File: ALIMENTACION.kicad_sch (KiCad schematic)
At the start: 12 parts, among them J5 5V_IN, U9 AP63203WU

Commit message: routing
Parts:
- added J20: 3V_IN, Connector_PinHeader_2.54mm:PinHeader_1x02_P2.54mm_Vertical, symbol Connector_Generic:Conn_01x02
- added R37, R38: 0, Resistor_SMD:R_0805_2012Metric, symbol Device:R
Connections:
- net +3.3V: now also R37.2, R38.2; no longer C30.1, C31.1, L2.2, U9.1 (FB)
- net GND: now also J20.2 (Pin_2)
- new net 3.3V_EXT: J20.1 (Pin_1), R37.1
- new net BUCK_3.3V: C30.1, C31.1, L2.2, R38.1, U9.1 (FB)
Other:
- moved on the sheet: C22

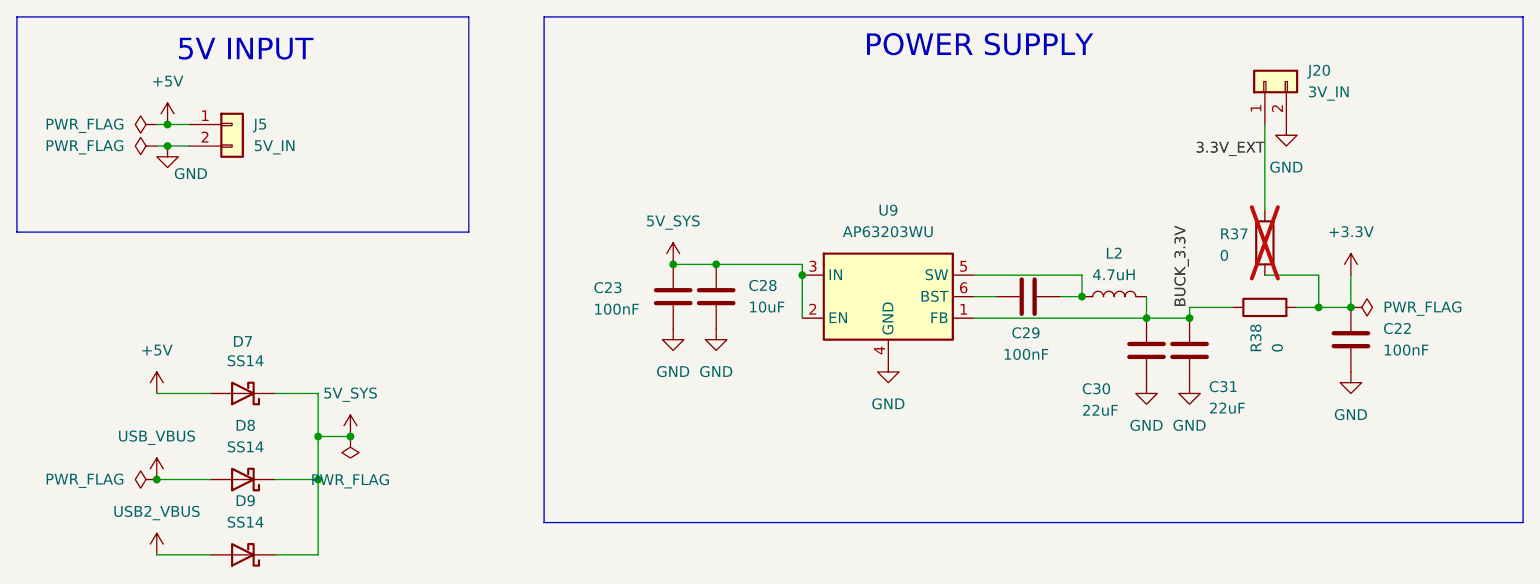
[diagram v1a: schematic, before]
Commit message: buck remplazado por regulador lineal
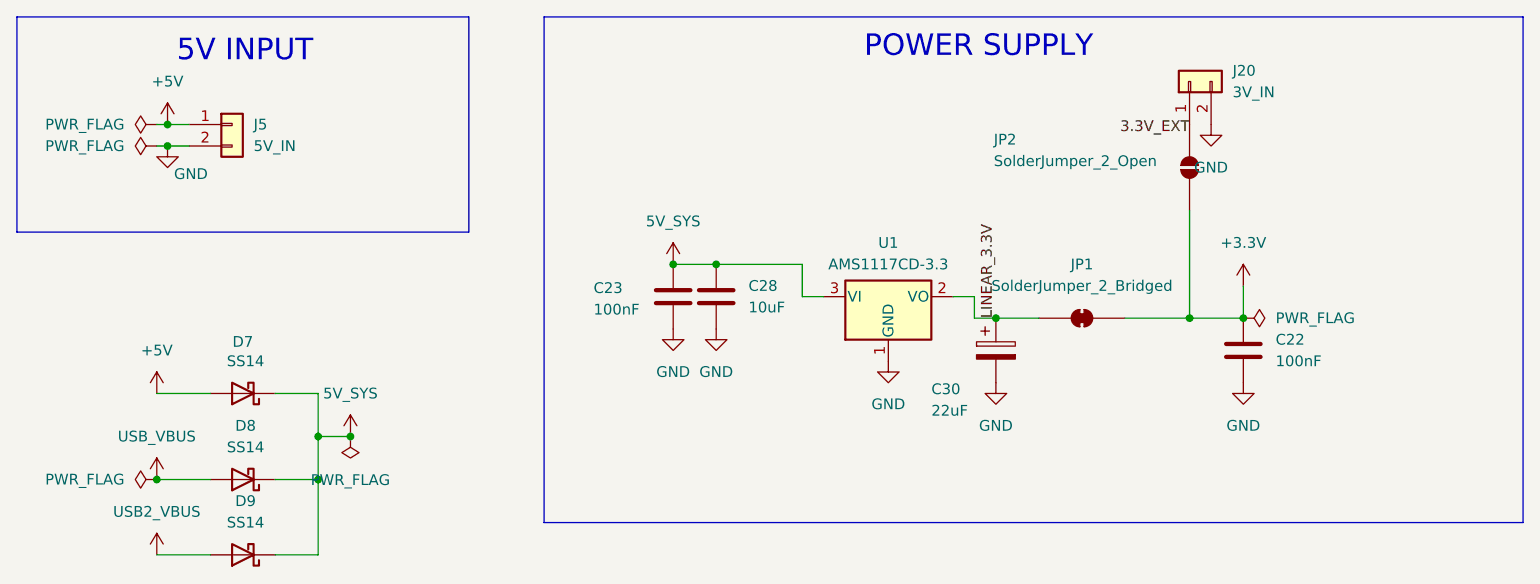
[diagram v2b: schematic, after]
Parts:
- removed C29: 100nF, Capacitor_SMD:C_0603_1608Metric, symbol Device:C
- removed C31: 22uF, Capacitor_SMD:C_0805_2012Metric, symbol Device:C
- removed L2: 4.7uH, Inductor_SMD:L_Changjiang_FXL0530, symbol Device:L
- removed R37, R38: 0, Resistor_SMD:R_0805_2012Metric, symbol Device:R
- removed U9: AP63203WU, Package_TO_SOT_SMD:TSOT-23-6, symbol Regulator_Switching:AP63203WU
- added JP1: SolderJumper_2_Bridged, Jumper:SolderJumper-2_P1.3mm_Bridged_RoundedPad1.0x1.5mm, symbol Jumper:SolderJumper_2_Bridged
- added JP2: SolderJumper_2_Open, Jumper:SolderJumper-2_P1.3mm_Open_RoundedPad1.0x1.5mm, symbol Jumper:SolderJumper_2_Open
- added U1: AMS1117CD-3.3, Package_TO_SOT_SMD:TO-252-3_TabPin2, symbol Regulator_Linear:AMS1117CD-3.3
- C30: footprint Capacitor_SMD:C_0805_2012Metric -> Capacitor_Tantalum_SMD:CP_EIA-3528-21_Kemet-B; symbol Device:C -> Device:C_Polarized; LCSC PN C45783 -> C117030; MPN CL21A226MAQNNNE -> T491B226K010AT; Manufacturer Samsung Electro-Mechanics -> KEMET; Manufacturer Part CL21A226MAQNNNE -> T491B226K010AT
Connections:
- net +3.3V: now also JP1.2 (B), JP2.2 (B)
- net 3.3V_EXT: no longer J20.1 (Pin_1)
- net 5V_SYS: now also U1.3 (VI)
- net GND: now also U1.1 (GND)
- net BUCK_3.3V renamed LINEAR_3.3V
- net LINEAR_3.3V: now also JP1.1 (A), U1.2 (VO)
- new net: J20.1 (Pin_1), JP2.1 (A)
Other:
- moved on the sheet: C22, J20

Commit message: removed usb_uart0
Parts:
- removed D8: SS14, Diode_SMD:D_SMA, symbol Diode:SS14

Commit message: fixes
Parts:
- JP1: now left out of the parts list
- U1: LCSC PN (none) -> C841796; MPN (none) -> AMS1117CD-3.3; Manufacturer (none) -> Advanced Monolithic Systems
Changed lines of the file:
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@@
 		(body_style 1)
 		(exclude_from_sim no)
-		(in_bom yes)
+		(in_bom no)
 		(on_board yes)
 		(in_pos_files yes)
@@
 			(hide yes)
 			(show_name no)
+			(do_not_autoplace no)
+			(effects
+				(font
+					(size 1.27 1.27)
+				)
+			)
+		)
+		(property "MPN" "AMS1117CD-3.3"
+			(at 0 0 0)
+			(hide yes)
+			(show_name no)
+			(do_not_autoplace no)
+			(effects
+				(font
+					(size 1.27 1.27)
+				)
+			)
+		)
+		(property "Manufacturer" "Advanced Monolithic Systems"
+			(at 0 0 0)
+			(hide yes)
+			(show_name no)
+			(do_not_autoplace no)
+			(effects
+				(font
+					(size 1.27 1.27)
+				)
+			)
+		)
+		(property "LCSC PN" "C841796"
+			(at 0 0 0)
+			(hide yes)
+			(show_name no)

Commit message: fixes
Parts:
- J20, J5: now left out of the parts list
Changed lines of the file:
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@@
 		(body_style 1)
 		(exclude_from_sim no)
-		(in_bom yes)
-		(on_board yes)
-		(in_pos_files yes)
+		(in_bom no)
+		(on_board yes)
+		(in_pos_files no)
 		(dnp no)
 		(fields_autoplaced yes)
@@
 		(body_style 1)
 		(exclude_from_sim no)
-		(in_bom yes)
-		(on_board yes)
-		(in_pos_files yes)
+		(in_bom no)
+		(on_board yes)
+		(in_pos_files no)
 		(dnp no)
 		(fields_autoplaced yes)

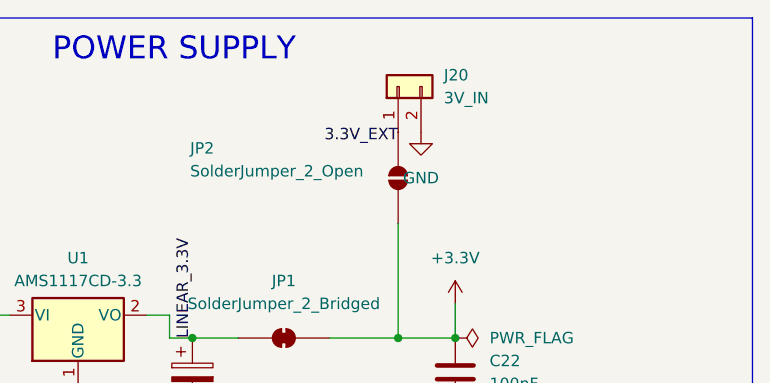
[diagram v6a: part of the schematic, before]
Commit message: Libera paquete JLCPCB SALUS v3
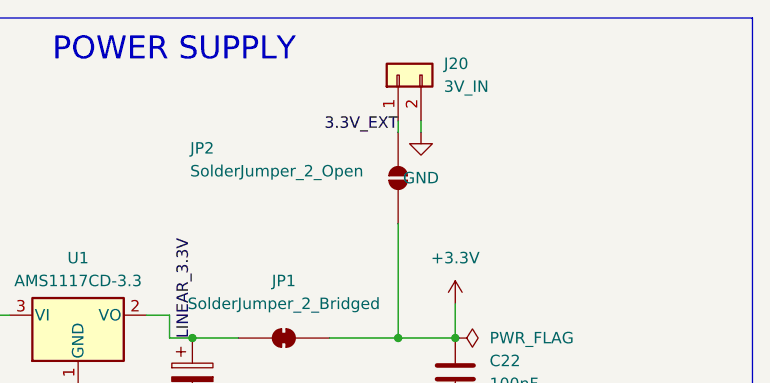
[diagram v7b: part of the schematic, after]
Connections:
- net 3.3V_EXT: now also J20.1 (Pin_1), JP2.1 (A)
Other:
- moved on the sheet: J20
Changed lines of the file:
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@@
+	(wire
+		(pts
+			(xy 167.64 59.69) (xy 167.64 60.96)
+		)
+		(stroke
+			(width 0)
+			(type default)
+		)
+	)
 	(wire
 		(pts
@@
 	(wire
 		(pts
+			(xy 165.1 59.69) (xy 165.1 60.96)
+		)
+		(stroke
+			(width 0)
+			(type default)
+		)
+	)
+	(wire
+		(pts
 			(xy 43.18 63.5) (xy 44.45 63.5)
 		)
@@
 	)
 	(label "3.3V_EXT"
-		(at 165.1 62.23 180)
+		(at 165.1 60.96 180)
 		(effects
 			(font
@@
 	(symbol
 		(lib_id "Connector_Generic:Conn_01x02")
-		(at 165.1 55.88 90)
+		(at 165.1 54.61 90)
 		(unit 1)
 		(body_style 1)
@@
 		(fields_autoplaced yes)
 		(property "Reference" "J20"
-			(at 170.18 54.6099 90)
+			(at 170.18 53.3399 90)
 			(show_name no)
 			(do_not_autoplace no)
@@
 		)
 		(property "Value" "3V_IN"
-			(at 170.18 57.1499 90)
+			(at 170.18 55.8799 90)
 			(show_name no)
 			(do_not_autoplace no)
@@
 		)
 		(property "Footprint" "Connector_PinHeader_2.54mm:PinHeader_1x02_P2.54mm_Vertical"
-			(at 165.1 55.88 0)
+			(at 165.1 54.61 0)
 			(hide yes)
 			(show_name no)
@@
 		)
 		(property "Datasheet" ""
-			(at 165.1 55.88 0)
+			(at 165.1 54.61 0)
 			(hide yes)
 			(show_name no)
@@
 		)
 		(property "Description" "Generic connector, single row, 01x02, script generated (kicad-library-utils/schlib/autogen/connector/)"
-			(at 165.1 55.88 0)
-			(hide yes)
-			(show_name no)
+			(at 165.1 54.61 0)
+			(hide yes)
+			(show_name no)

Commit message: Consolida pasivos Basic y valida filtro de acelerador
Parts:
- C22, C23: LCSC PN C1590 -> C14663; MPN CL10B104KA8NNNC -> CC0603KRX7R9BB104; Manufacturer Samsung Electro-Mechanics -> Yageo; Manufacturer Part CL10B104KA8NNNC -> CC0603KRX7R9BB104
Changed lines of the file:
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@@
 			)
 		)
-		(property "LCSC PN" "C1590"
+		(property "LCSC PN" "C14663"
 			(at -101.6 -64.77 0)
 			(hide yes)
@@
 			)
 		)
-		(property "Manufacturer" "Samsung Electro-Mechanics"
+		(property "Manufacturer" "Yageo"
 			(at -101.6 -64.77 0)
 			(hide yes)
@@
 			)
 		)
-		(property "Manufacturer Part" "CL10B104KA8NNNC"
+		(property "Manufacturer Part" "CC0603KRX7R9BB104"
 			(at -101.6 -64.77 0)
 			(hide yes)
@@
 			)
 		)
-		(property "MPN" "CL10B104KA8NNNC"
+		(property "MPN" "CC0603KRX7R9BB104"
 			(at -101.6 -64.77 0)
 			(hide yes)
@@
 			)
 		)
-		(property "LCSC PN" "C1590"
+		(property "LCSC PN" "C14663"
 			(at -168.91 -71.12 0)
 			(hide yes)
@@
 			)
 		)
-		(property "Manufacturer" "Samsung Electro-Mechanics"
+		(property "Manufacturer" "Yageo"
 			(at -168.91 -71.12 0)
 			(hide yes)
@@
 			)
 		)
-		(property "Manufacturer Part" "CL10B104KA8NNNC"
+		(property "Manufacturer Part" "CC0603KRX7R9BB104"
 			(at -168.91 -71.12 0)
 			(hide yes)
@@
 			)
 		)
-		(property "MPN" "CL10B104KA8NNNC"
+		(property "MPN" "CC0603KRX7R9BB104"
 			(at -168.91 -71.12 0)
 			(hide yes)
